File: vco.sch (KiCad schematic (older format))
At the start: 0 parts

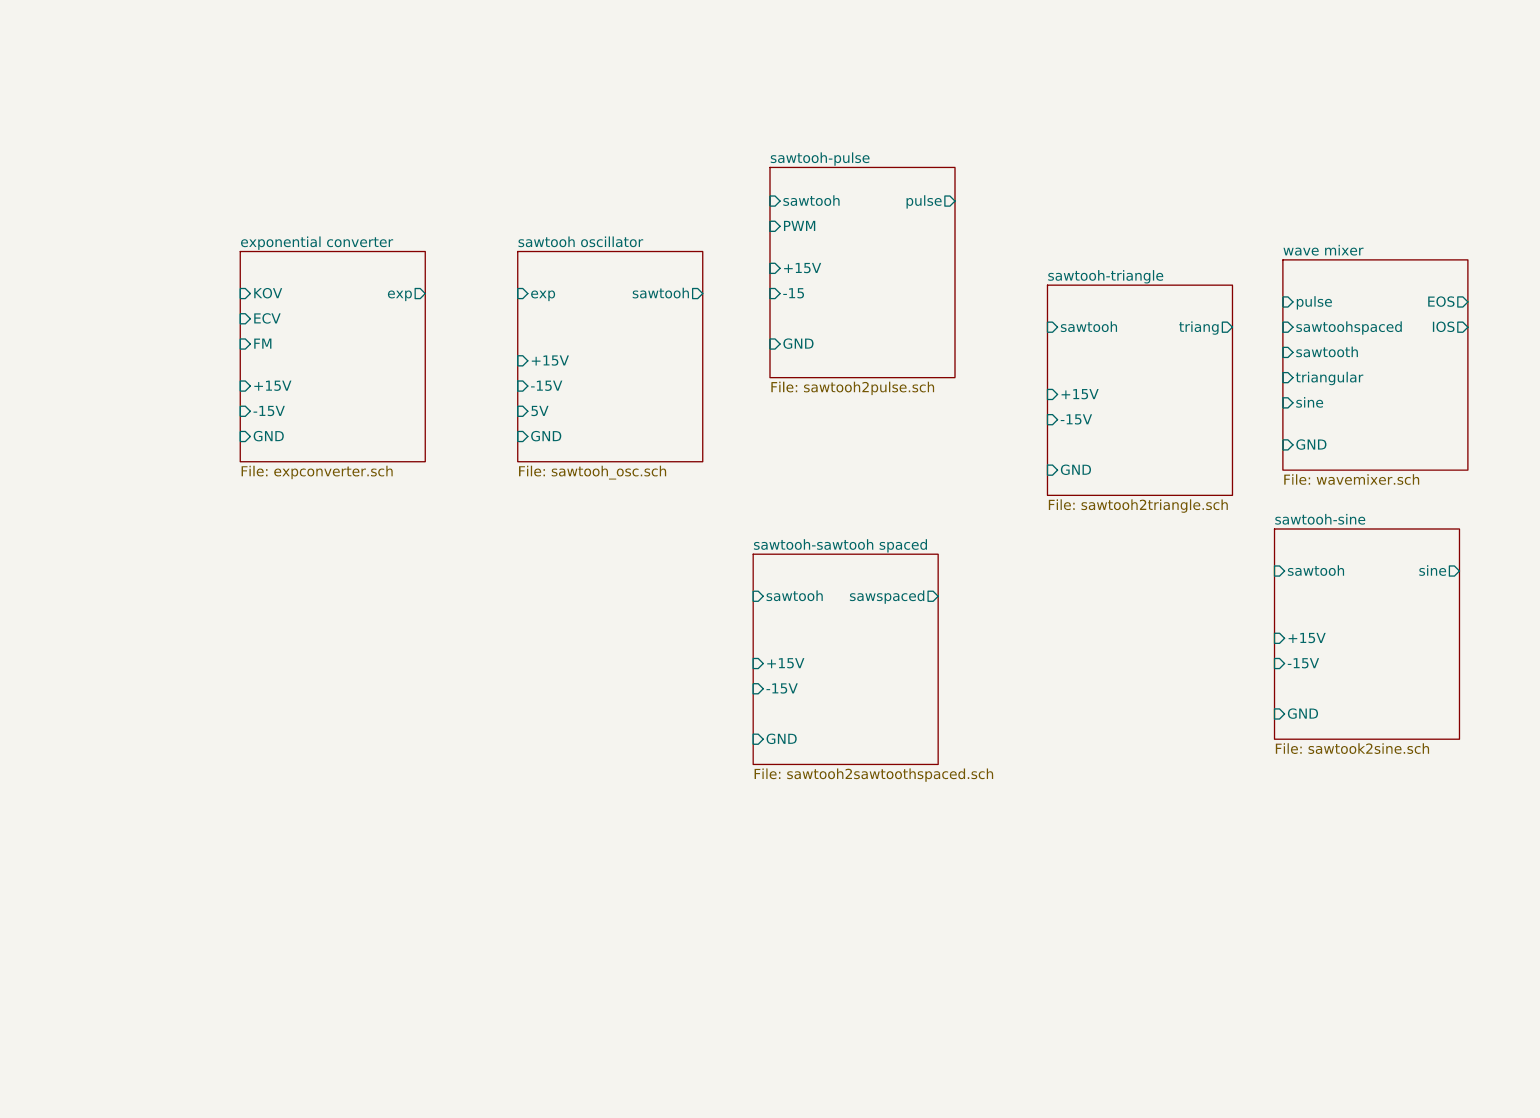
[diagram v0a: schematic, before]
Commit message: añado alimentacion
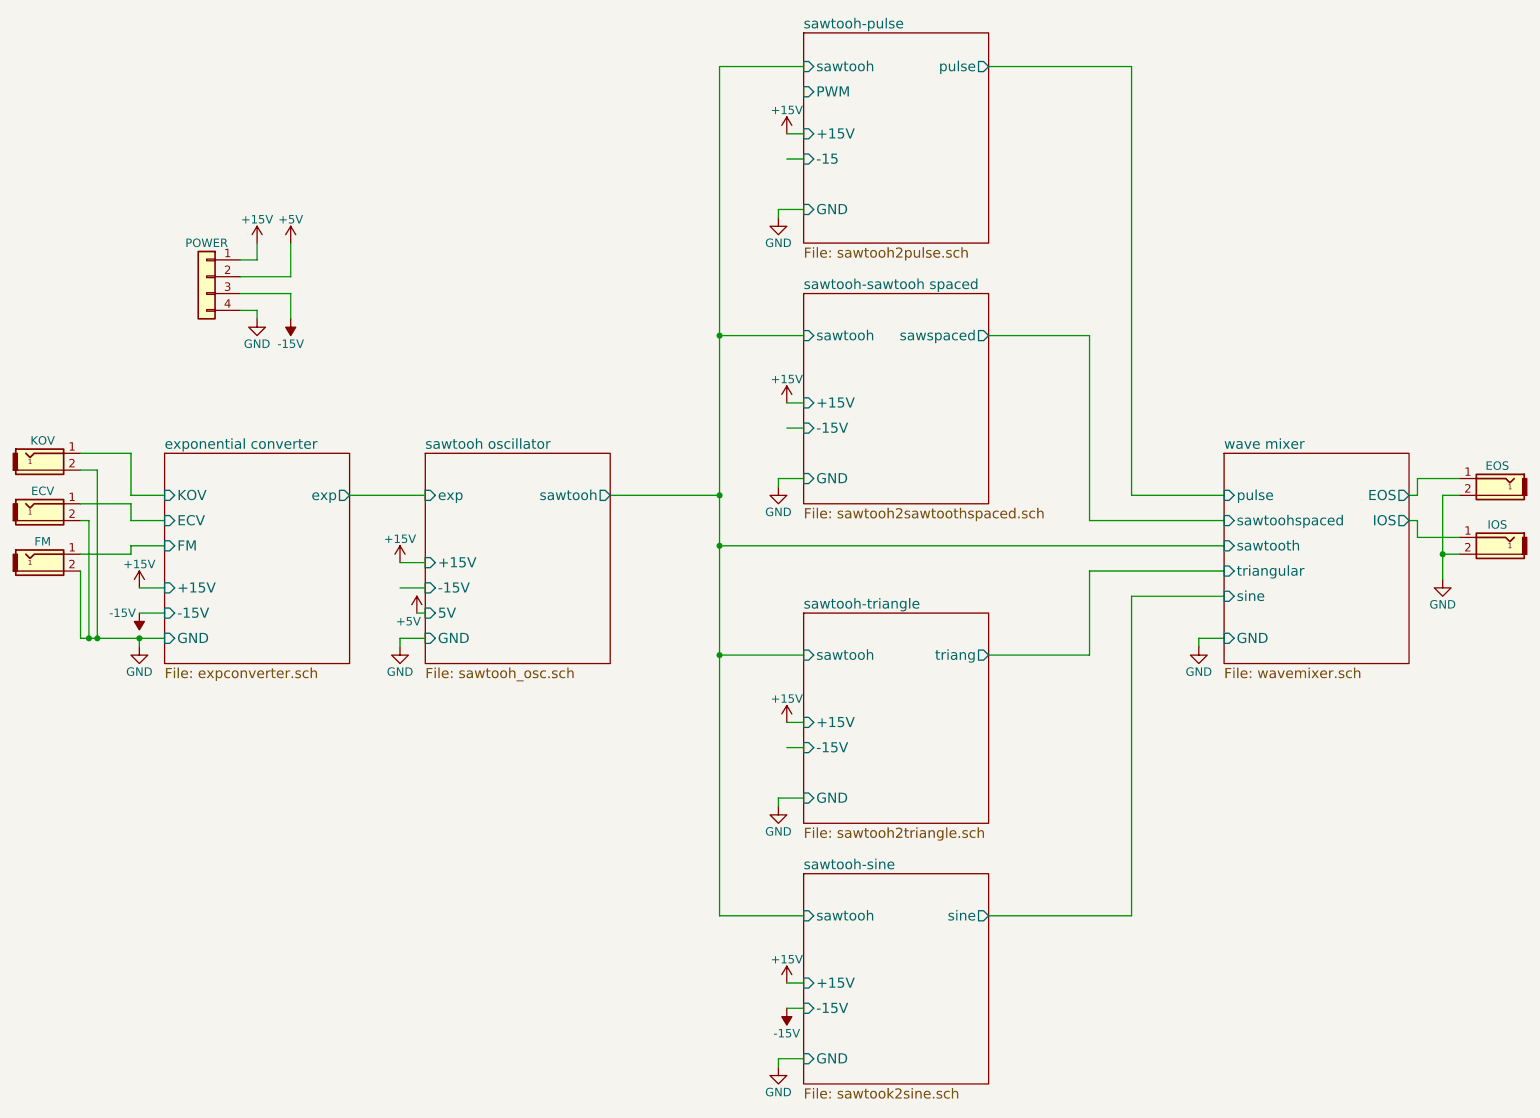
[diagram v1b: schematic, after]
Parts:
- added ECV, EOS, FM, IOS, KOV: Audio-Jack-2, symbol Audio-Jack-2
- added POWER: Conn_01x04, symbol Conn_01x04
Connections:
- net labels added: +15V, +5V, -15V, GND
- wire segments 0 -> 86
